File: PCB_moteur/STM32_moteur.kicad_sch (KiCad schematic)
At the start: 54 parts, among them U1 STM32F103CBT6

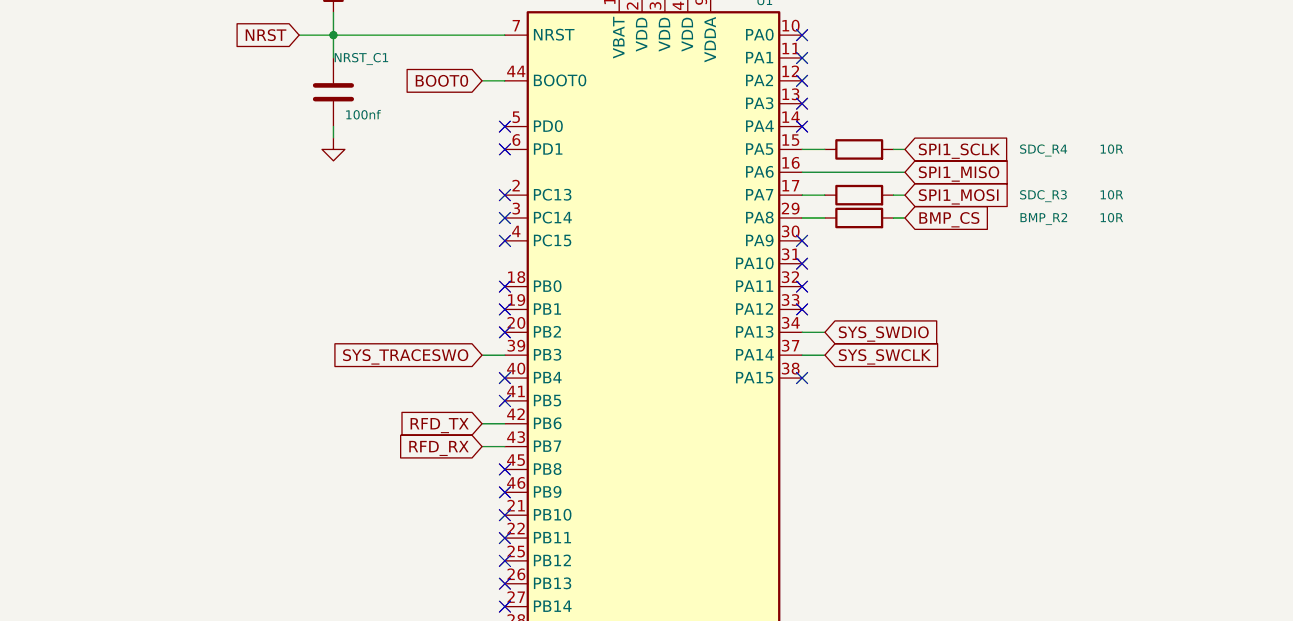
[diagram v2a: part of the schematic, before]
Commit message: wip: change 4 pyros -> 2 pyros
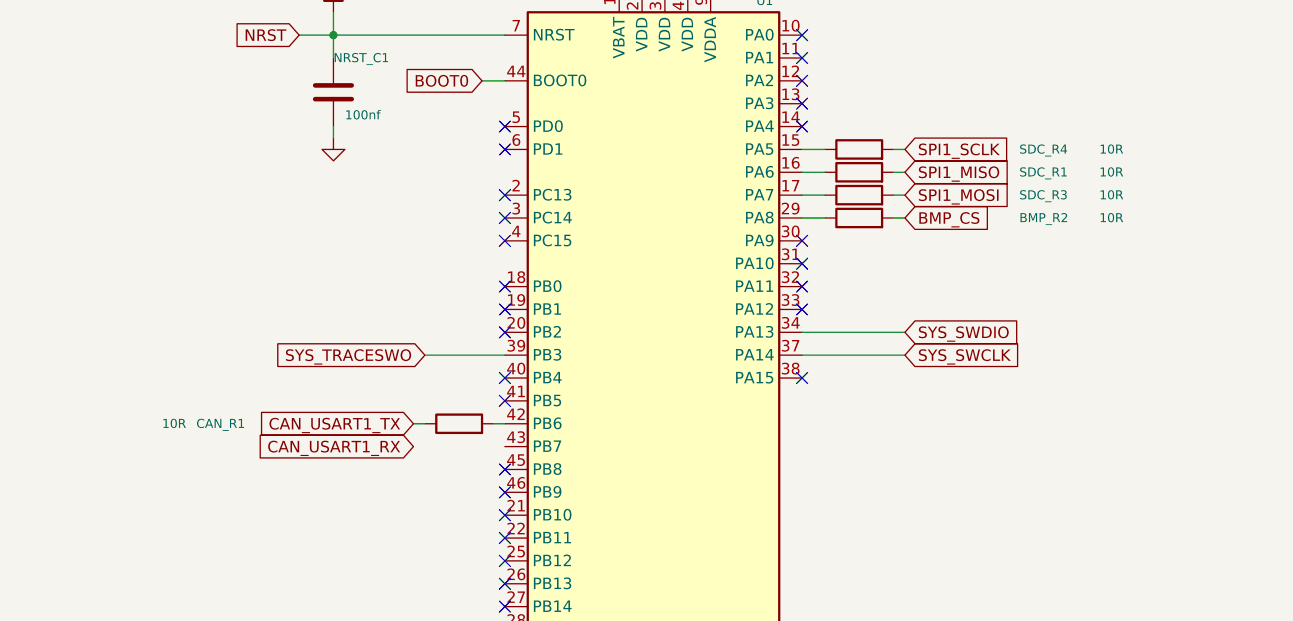
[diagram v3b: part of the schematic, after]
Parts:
- added CAN_R1, SDC_R1: 10R, Resistor_SMD:R_0805_2012Metric, symbol Device:R
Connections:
- net SPI1_MISO: now also SDC_R1.2; no longer U1.16 (PA6)
- net RFD_RX: no longer names the net of U1.43 (PB7)
- net RFD_TX: no longer names the net of U1.42 (PB6)
- net RFD_TX: now also CAN_R1.2
- new net: SDC_R1.1, U1.16 (PA6)
- new net CAN_USART1_TX: CAN_R1.1
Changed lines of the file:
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@@
 	(wire
 		(pts
+			(xy 184.15 46.99) (xy 185.42 46.99)
+		)
+		(stroke
+			(width 0)
+			(type default)
+		)
+	)
+	(wire
+		(pts
 			(xy 251.46 64.77) (xy 259.08 64.77)
 		)
@@
 	(wire
 		(pts
-			(xy 138.43 67.31) (xy 140.97 67.31)
+			(xy 132.08 67.31) (xy 140.97 67.31)
 		)
 		(stroke
@@
 	(wire
 		(pts
-			(xy 138.43 74.93) (xy 140.97 74.93)
+			(xy 48.26 63.5) (xy 49.53 63.5)
 		)
 		(stroke
@@
 	(wire
 		(pts
-			(xy 48.26 63.5) (xy 49.53 63.5)
+			(xy 243.84 64.77) (xy 251.46 64.77)
 		)
 		(stroke
@@
 	(wire
 		(pts
-			(xy 243.84 64.77) (xy 251.46 64.77)
+			(xy 130.81 74.93) (xy 132.08 74.93)
 		)
 		(stroke
@@
 	(wire
 		(pts
-			(xy 43.18 153.67) (xy 40.64 153.67)
+			(xy 139.7 74.93) (xy 140.97 74.93)
 		)
 		(stroke
@@
 	(wire
 		(pts
-			(xy 43.18 163.83) (xy 40.64 163.83)
+			(xy 43.18 153.67) (xy 40.64 153.67)
 		)
 		(stroke
@@
 	(wire
 		(pts
-			(xy 184.15 44.45) (xy 185.42 44.45)
+			(xy 43.18 163.83) (xy 40.64 163.83)
 		)
 		(stroke
@@
 	(wire
 		(pts
-			(xy 251.46 52.07) (xy 251.46 54.61)
+			(xy 184.15 44.45) (xy 185.42 44.45)
 		)
 		(stroke
@@
 	(wire
 		(pts
-			(xy 265.43 87.63) (xy 265.43 91.44)
+			(xy 251.46 52.07) (xy 251.46 54.61)
 		)
 		(stroke
@@
 	(wire
 		(pts
-			(xy 62.23 163.83) (xy 64.77 163.83)
+			(xy 265.43 87.63) (xy 265.43 91.44)
 		)
 		(stroke
@@
 	(wire
 		(pts
-			(xy 265.43 76.2) (xy 265.43 77.47)
+			(xy 62.23 163.83) (xy 64.77 163.83)
 		)
 		(stroke
@@
 	(wire
 		(pts
-			(xy 265.43 77.47) (xy 265.43 80.01)
+			(xy 265.43 76.2) (xy 265.43 77.47)
 		)
 		(stroke
@@
 	(wire
 		(pts
-			(xy 138.43 77.47) (xy 140.97 77.47)
+			(xy 265.43 77.47) (xy 265.43 80.01)
 		)
 		(stroke
@@
 	(wire
 		(pts
-			(xy 173.99 67.31) (xy 176.53 67.31)
+			(xy 173.99 67.31) (xy 185.42 67.31)
 		)
 		(stroke
@@
 	(wire
 		(pts
-			(xy 173.99 46.99) (xy 185.42 46.99)
+			(xy 173.99 46.99) (xy 176.53 46.99)
 		)
 		(stroke
@@
 	(wire
 		(pts
-			(xy 173.99 64.77) (xy 176.53 64.77)
+			(xy 173.99 64.77) (xy 185.42 64.77)
 		)
 		(stroke
@@
 	(global_label "SYS_SWDIO"
 		(shape input)
-		(at 176.53 64.77 0)
+		(at 185.42 64.77 0)
 		(fields_autoplaced yes)
 		(effects
@@
 		)
 		(property "Intersheetrefs" "${INTERSHEET_REFS}"
-			(at 189.8566 64.77 0)
+			(at 198.7466 64.77 0)
 			(effects
 				(font
@@
 		)
 	)
-	(global_label "RFD_TX"
-		(shape input)
-		(at 138.43 74.93 180)
-		(fields_autoplaced yes)
-		(effects
-			(font
-				(size 1.27 1.27)
-			)
-			(justify right)
-		)
-		(property "Intersheetrefs" "${INTERSHEET_REFS}"
-			(at 128.6715 74.93 0)
-			(effects
-				(font
-					(size 1.27 1.27)
-				)
-				(justify right)
-				(hide yes)
-			)
-		)
-	)
 	(global_label "MEM_QSPI_IO0"
 		(shape input)
@@
 	(global_label "SYS_TRACESWO"
 		(shape input)
-		(at 138.43 67.31 180)
+		(at 132.08 67.31 180)
 		(fields_autoplaced yes)
 		(effects
@@
 		)
 		(property "Intersheetrefs" "${INTERSHEET_REFS}"
-			(at 121.233 67.31 0)
+			(at 114.883 67.31 0)
 			(effects
 				(font
@@
 		)
 	)
+	(global_label "CAN_USART1_TX"
+		(shape input)
+		(at 130.81 74.93 180)
+		(fields_autoplaced yes)
+		(effects
+			(font
+				(size 1.27 1.27)
+			)
+			(justify right)
+		)
+		(property "Intersheetrefs" "${INTERSHEET_REFS}"
+			(at 112.9477 74.93 0)
+			(effects
+				(font
+					(size 1.27 1.27)
+				)
+				(justify right)
+				(hide yes)
+			)
+		)
+	)
+	(global_label "CAN_USART1_RX"
+		(shape input)
+		(at 130.81 77.47 180)
+		(fields_autoplaced yes)
+		(effects
+			(font
+				(size 1.27 1.27)
+			)
+			(justify right)
+		)
+		(property "Intersheetrefs" "${INTERSHEET_REFS}"
+			(at 112.6453 77.47 0)
+			(effects
+				(font
+					(size 1.27 1.27)
+				)
+				(justify right)
+				(hide yes)
+			)
+		)
+	)
 	(global_label "EXTEND_IO2"
 		(shape input)
@@
 	(global_label "SYS_SWCLK"
 		(shape input)
-		(at 176.53 67.31 0)
+		(at 185.42 67.31 0)
 		(fields_autoplaced yes)
 		(effects
@@
 		)
 		(property "Intersheetrefs" "${INTERSHEET_REFS}"
-			(at 190.2194 67.31 0)
+			(at 199.1094 67.31 0)
 			(effects
 				(font
@@
 		)
 	)
-	(global_label "RFD_RX"
-		(shape input)
-		(at 138.43 77.47 180)
-		(fields_autoplaced yes)
-		(effects
-			(font
-				(size 1.27 1.27)
-			)
-			(justify right)
-		)
-		(property "Intersheetrefs" "${INTERSHEET_REFS}"
-			(at 128.3691 77.47 0)
-			(effects
-				(font
-					(size 1.27 1.27)
-				)
-				(justify right)
-				(hide yes)
-			)
-		)
-	)
 	(global_label "CriticalLED"
 		(shape input)
@@
 	)
 	(symbol
+		(lib_id "Device:R")
+		(at 180.34 46.99 90)
+		(unit 1)
+		(exclude_from_sim no)
+		(in_bom yes)
+		(on_board yes)
+		(dnp no)
+		(property "Reference" "SDC_R1"
+			(at 198.12 46.99 90)
+			(effects
+				(font
+					(size 1 1)
+				)
+				(justify right)
+			)
+		)
+		(property "Value" "10R"
+			(at 207.01 46.99 90)
+			(effects
+				(font
+					(size 1 1)
+				)
+				(justify right)
+			)
+		)
+		(property "Footprint" "Resistor_SMD:R_0805_2012Metric"
+			(at 180.34 48.768 90)
+			(effects
+				(font
+					(size 1 1)
+				)
+				(hide yes)
+			)
+		)
+		(property "Datasheet" "~"
+			(at 180.34 46.99 0)
+			(effects
+				(font
+					(size 1 1)
+				)
+				(hide yes)
+			)
+		)
+		(property "Description" ""
+			(at 180.34 46.99 0)
+			(effects
+				(font
+					(size 1.27 1.27)
+				)
+			)
+		)
+		(pin "1"
+		)
+		(pin "2"
+		)
+		(instances
+			(project "PCB_moteur"
+				(path "/b0d87684-7b1c-41d8-8358-755aa327573e/753d1783-c2f5-4012-bbb8-3f4eadf066f6"
+					(reference "SDC_R1")
+					(unit 1)
+				)
+			)
+		)
+	)
+	(symbol
 		(lib_id "Device:LED")
 		(at 54.61 83.82 180)
@@
 					(unit 1)
 				)
+			)
+		)
+	)
+	(symbol
+		(lib_id "Device:R")
+		(at 135.89 74.93 90)
+		(unit 1)
+		(exclude_from_sim no)
+		(in_bom yes)
+		(on_board yes)
+		(dnp no)
+		(property "Reference" "CAN_R1"
+			(at 106.68 74.93 90)
+			(effects
+				(font
+					(size 1 1)
+				)
+				(justify right)
+			)
+		)
+		(property "Value" "10R"
+			(at 102.87 74.93 90)
+			(effects
+				(font
+					(size 1 1)
+				)
+				(justify right)
+			)
+		)
+		(property "Footprint" "Resistor_SMD:R_0805_2012Metric"
+			(at 135.89 76.708 90)
+			(effects
+				(font
+					(size 1 1)
+				)
+				(hide yes)
+			)
+		)
+		(property "Datasheet" "~"
+			(at 135.89 74.93 0)
+			(effects
+				(font
+					(size 1 1)
+				)
+				(hide yes)
+			)
+		)
+		(property "Description" ""
+			(at 135.89 74.93 0)
+			(effects
+				(font
+					(size 1.27 1.27)
+				)
+			)
+		)
+		(pin "1"
+		)
+		(pin "2"
+		)
+		(instances
+			(project "PCB_moteur"
+				(path "/b0d87684-7b1c-41d8-8358-755aa327573e/753d1783-c2f5-4012-bbb8-3f4eadf066f6"
+					(reference "CAN_R1")
+					(unit 1)
+				)

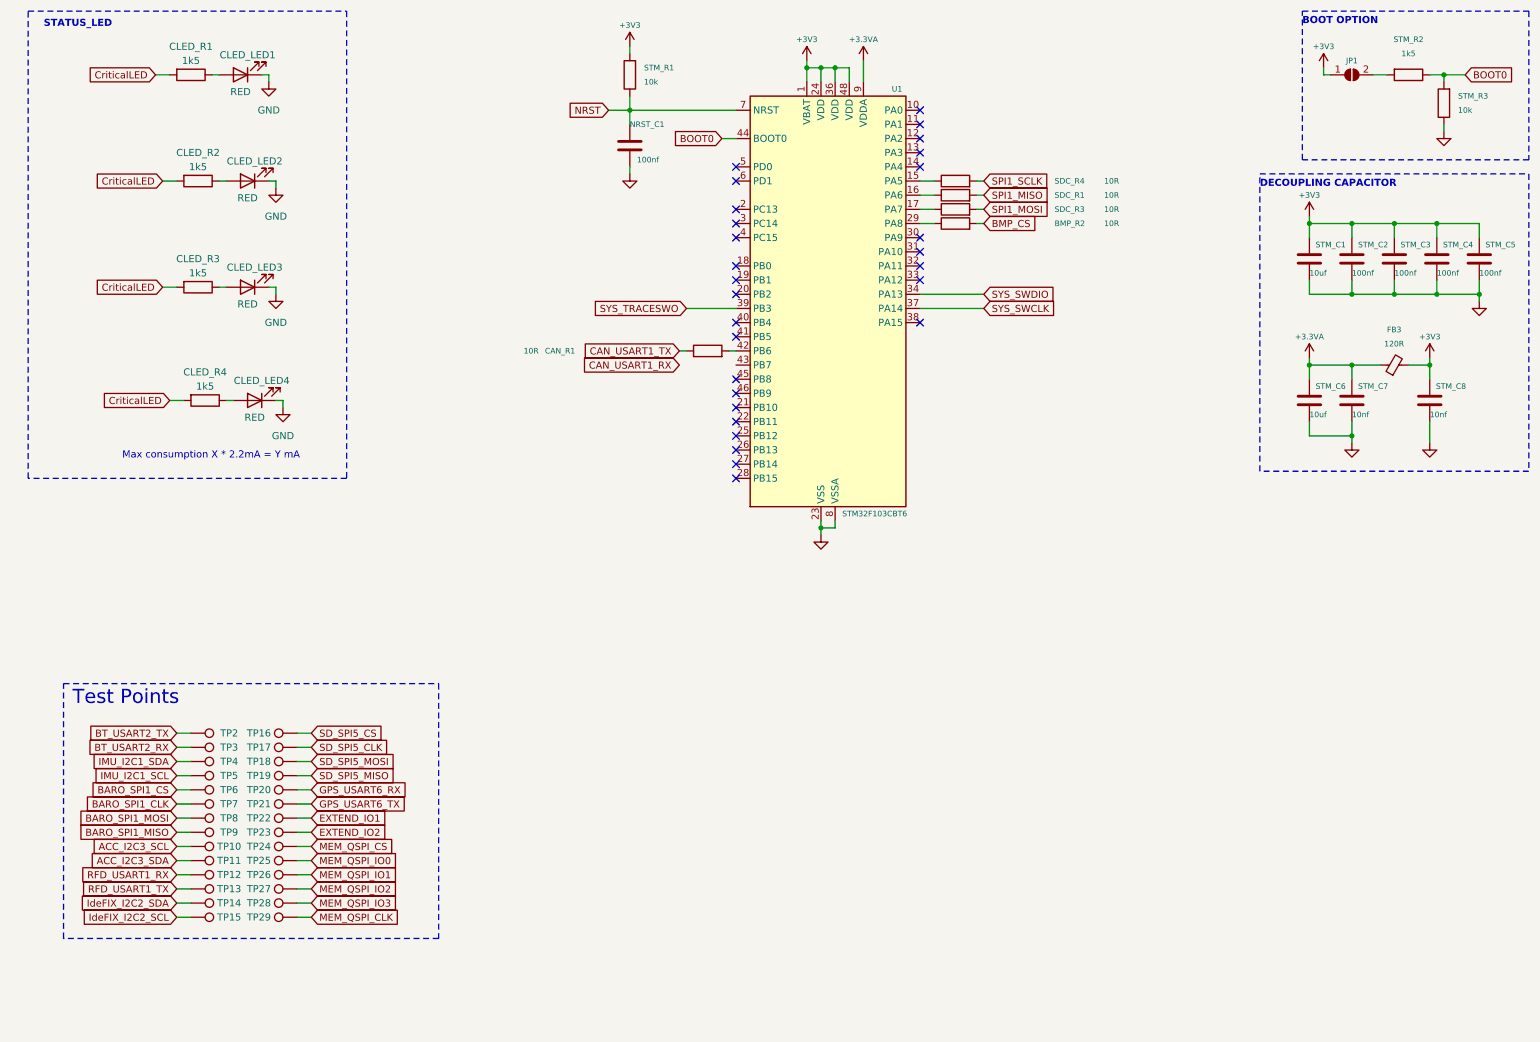
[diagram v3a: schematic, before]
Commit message: fix: power supply + add LED RG + add mounting holes + change 6pins header SWD connector + pyros
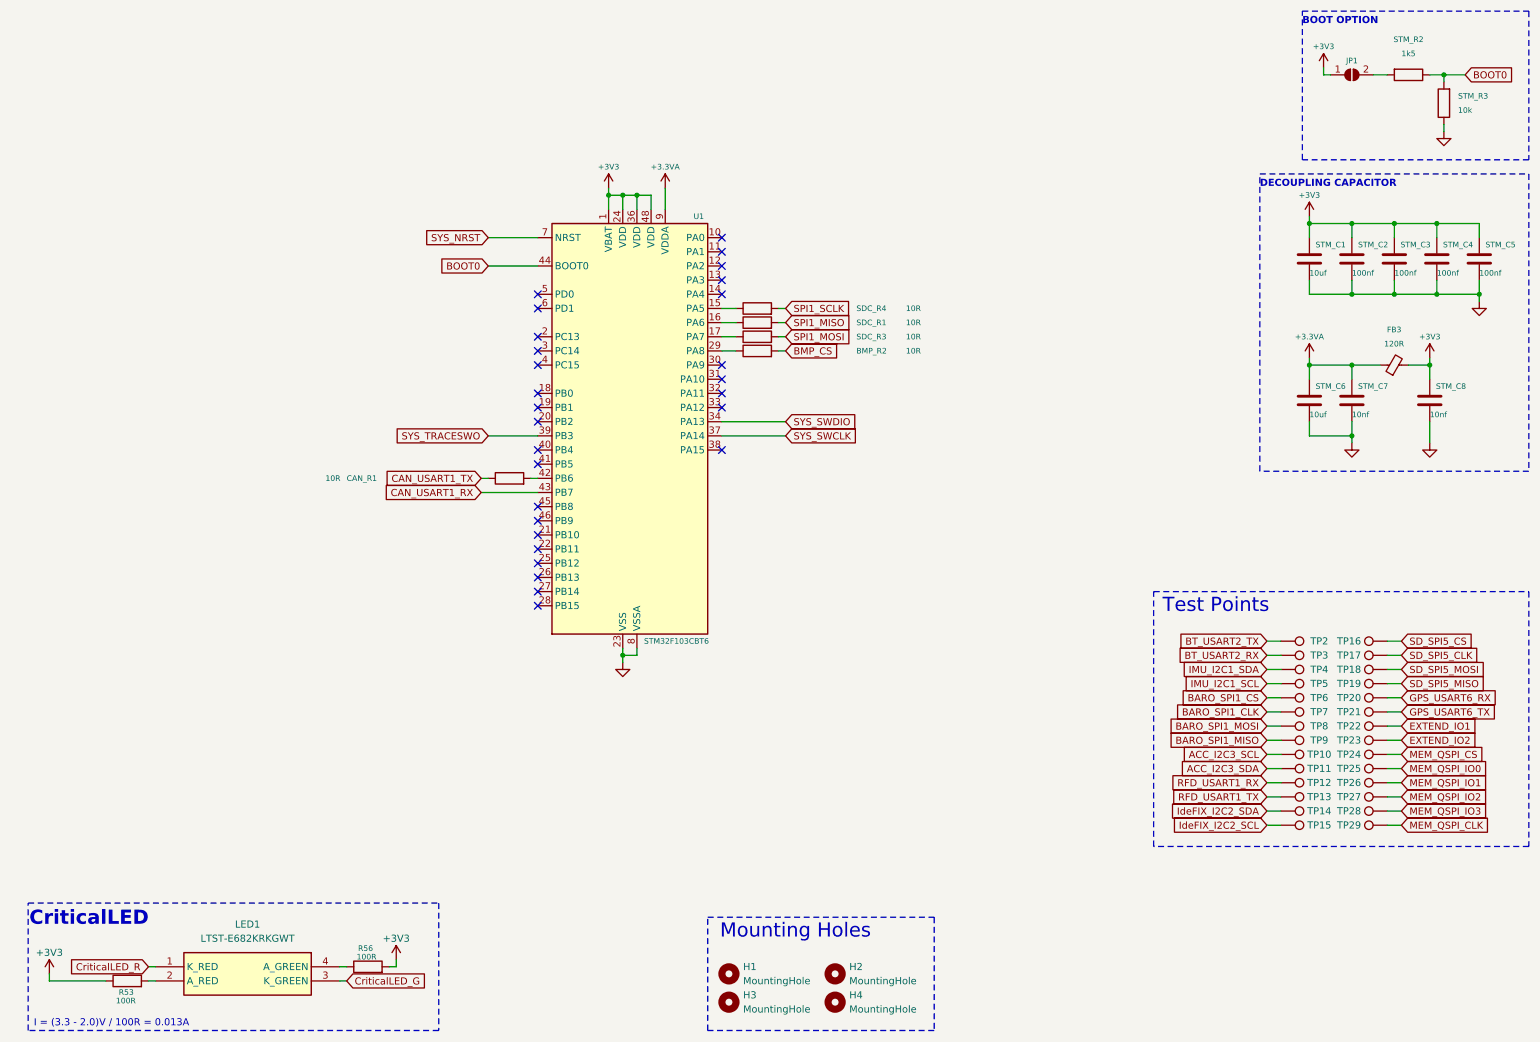
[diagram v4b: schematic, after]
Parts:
- removed CLED_LED1, CLED_LED2, CLED_LED3, CLED_LED4: RED, LED_SMD:LED_0603_1608Metric, symbol Device:LED
- removed CLED_R1, CLED_R2, CLED_R3, CLED_R4: 1k5, Resistor_SMD:R_0603_1608Metric, symbol Device:R
- removed NRST_C1: 100nf, Capacitor_SMD:C_0805_2012Metric, symbol Device:C
- removed STM_R1: 10k, Resistor_SMD:R_0805_2012Metric, symbol Device:R
- added H1, H2, H3, H4: MountingHole, symbol Mechanical:MountingHole
- added LED1: LTST-E682KRKGWT, LTSTE683RGBW, symbol pcb_moteur:LTST-E682KRKGWT
- added R53, R56: 100R, Resistor_SMD:R_0603_1608Metric, symbol Device:R
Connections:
- net +3V3: now also R53.1, R56.2
- net CAN_USART1_RX: now also U1.43 (PB7)
- net NRST renamed SYS_NRST
- new net: LED1.4 (A_GREEN), R56.1
- new net: LED1.2 (A_RED), R53.2
- new net CriticalLED_G: LED1.3 (K_GREEN)
- new net CriticalLED_R: LED1.1 (K_RED)
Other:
- note added: "CriticalLED"
- note added: "I = (3.3 - 2.0)V / 100R = 0.013A"
- note added: "Mounting Holes"
- note removed: "Max consumption X * 2.2mA = Y mA"
- note removed: "STATUS_LED"
- moved on the sheet: BMP_R2, CAN_R1, SDC_R1, SDC_R3, SDC_R4, TP10, TP11, TP12, TP13, TP14, TP15, TP16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

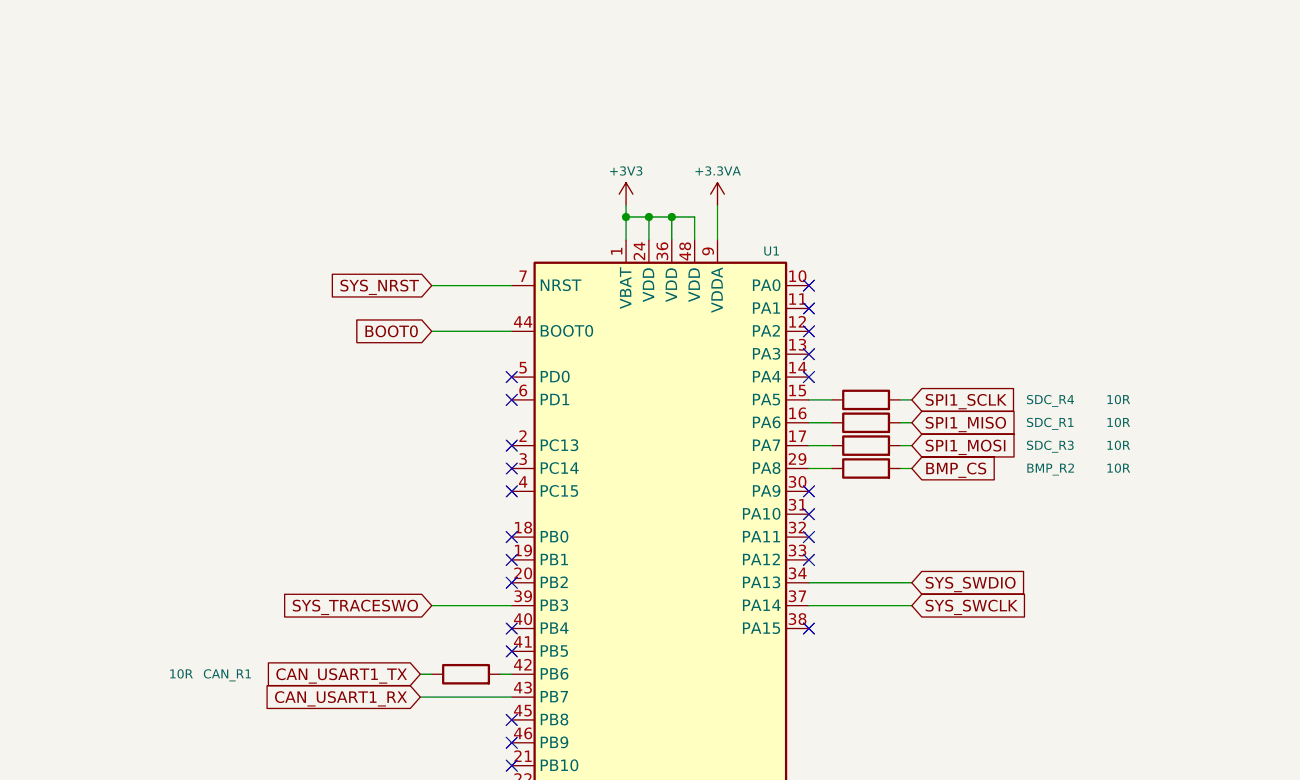
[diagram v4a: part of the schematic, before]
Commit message: fix: resistors + capacitances power supply
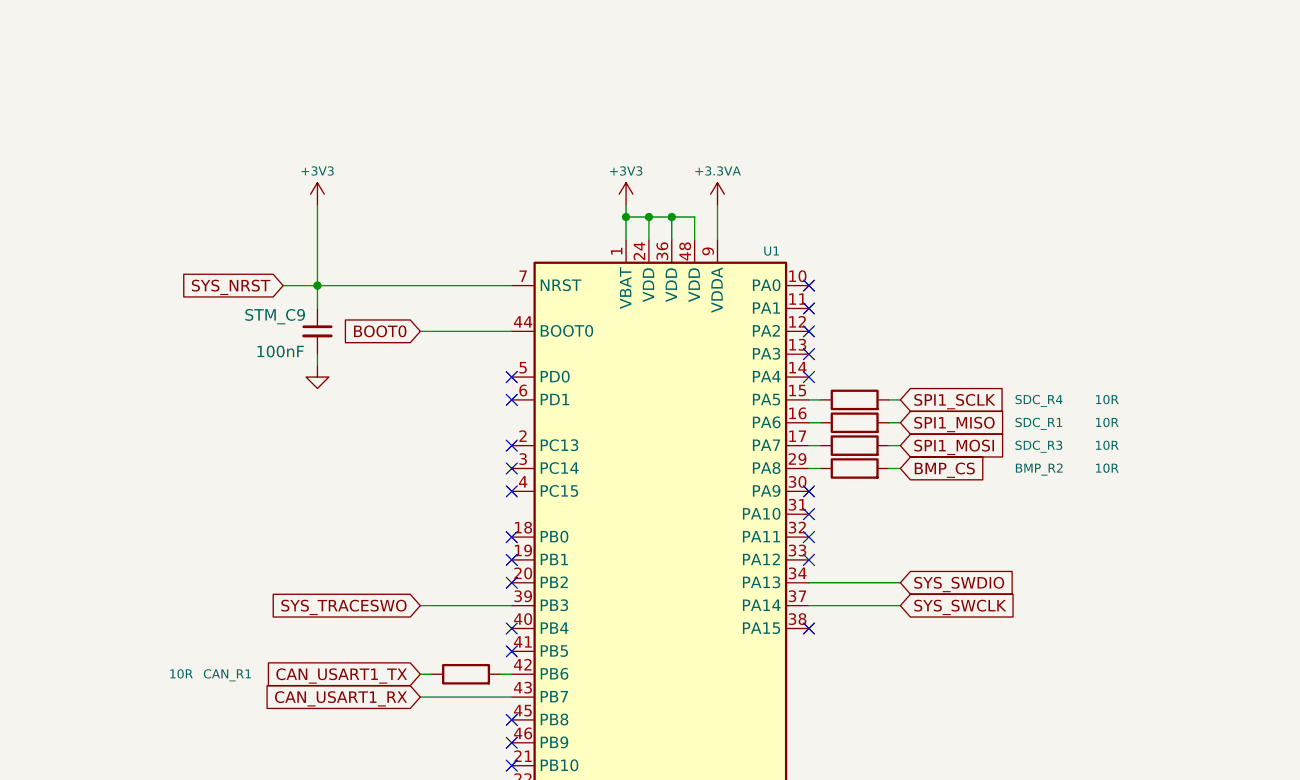
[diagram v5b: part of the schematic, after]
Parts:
- added STM_C9: 100nF, Capacitor_SMD:C_0603_1608Metric, symbol Device:C_Small
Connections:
- net SYS_NRST is gone; now on net +3V3: U1.7 (NRST)
- net +3V3: now also STM_C9.1
- net GND: now also STM_C9.2
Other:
- moved on the sheet: BMP_R2, SDC_R1, SDC_R3, SDC_R4
